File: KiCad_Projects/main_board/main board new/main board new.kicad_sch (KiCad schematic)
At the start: 71 parts

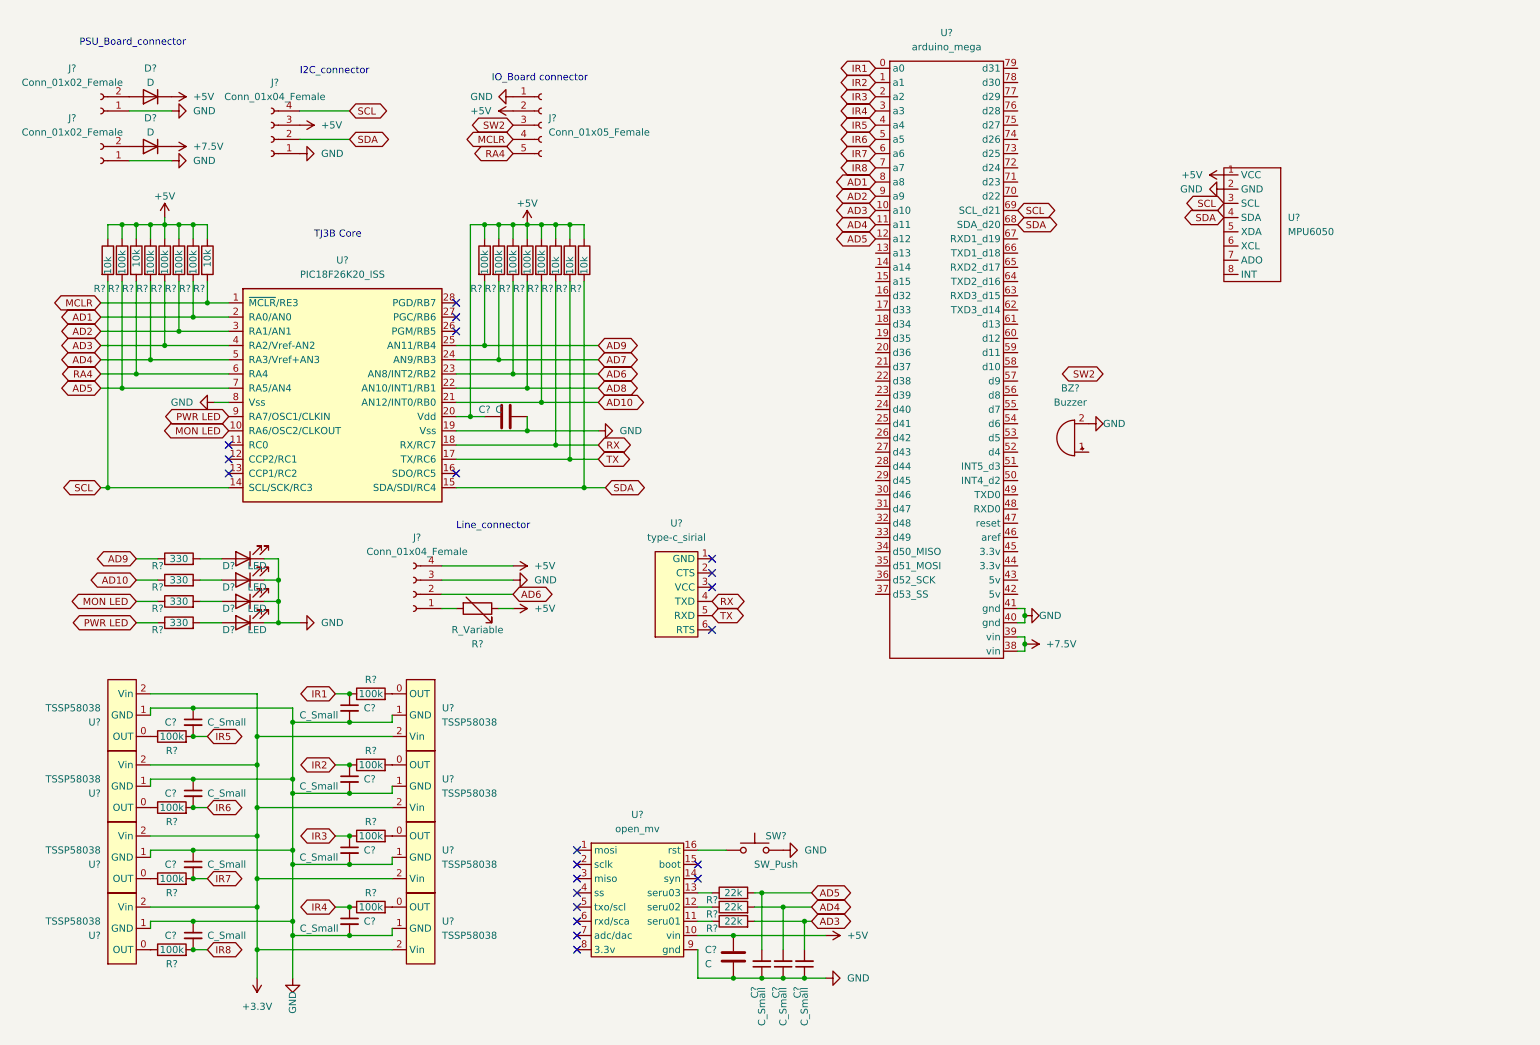
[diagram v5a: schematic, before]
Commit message: 基板データの更新
新メイン基板の更新
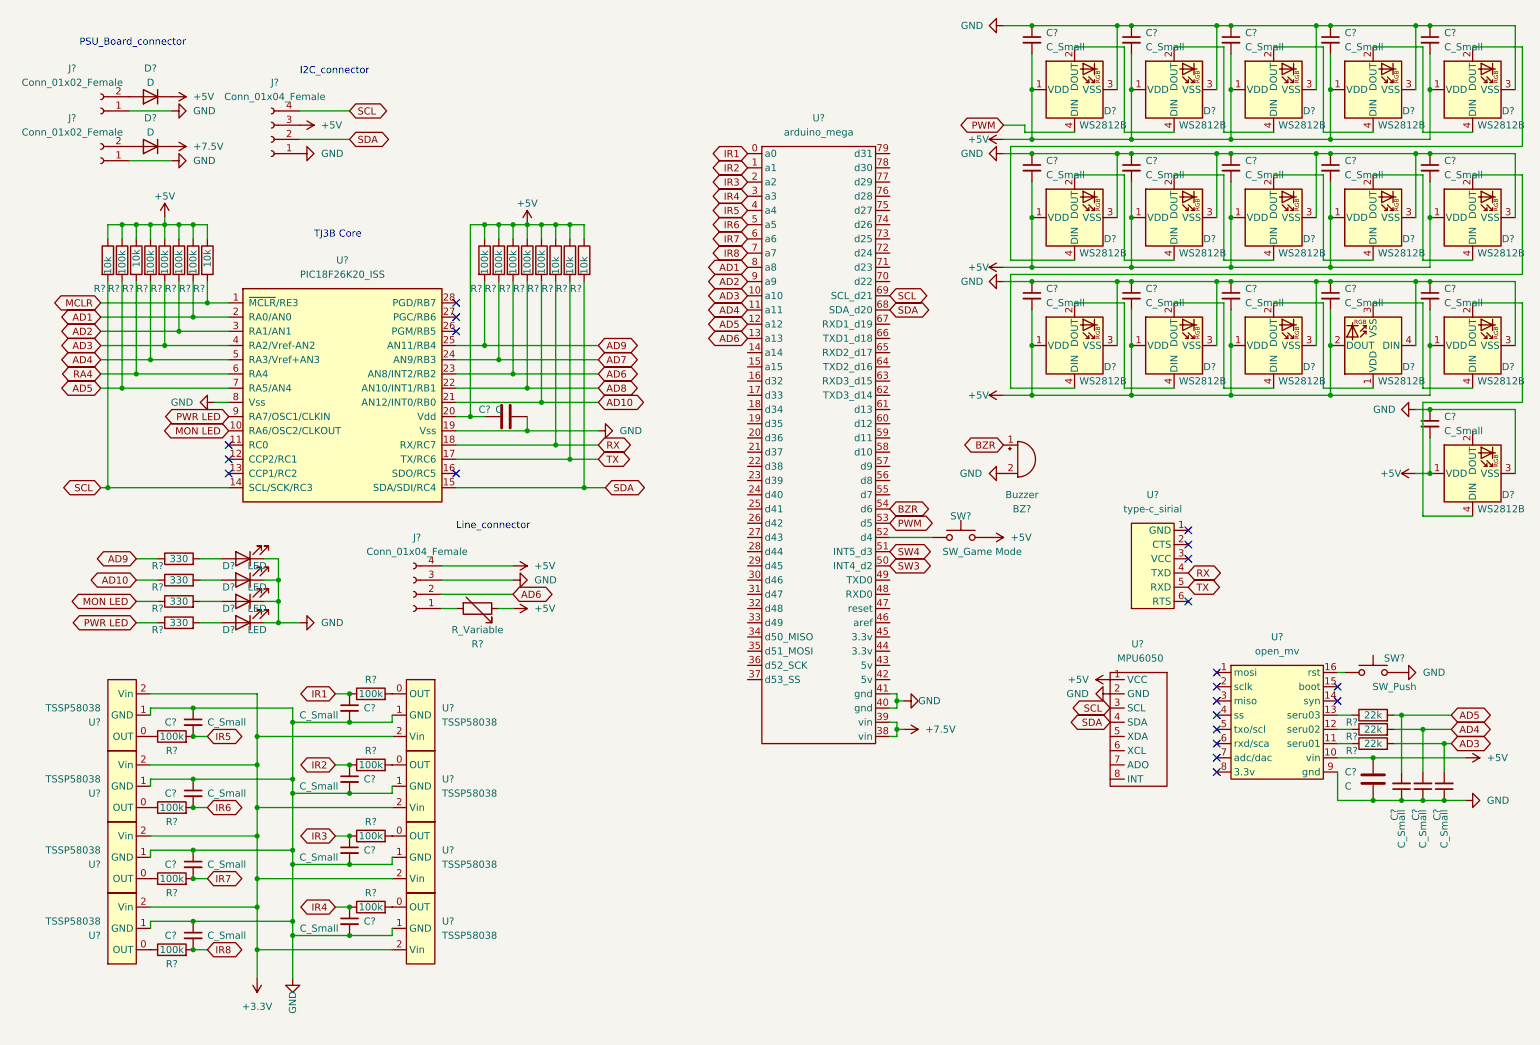
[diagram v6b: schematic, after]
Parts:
- removed J?: Conn_01x05_Female, Connector_JST:JST_XH_B5B-XH-A_1x05_P2.50mm_Vertical, symbol Connector:Conn_01x05_Female
- added C? (x16): C_Small, symbol Device:C_Small
- added D? (x16): WS2812B, LED_SMD:LED_WS2812B_PLCC4_5.0x5.0mm_P3.2mm, symbol LED:WS2812B
- added SW?: SW_Game Mode, Button_Switch_THT:SW_PUSH_6mm_H5mm, symbol Switch:SW_Push
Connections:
- net +5V: now also C?.2, C?.2, C?.2, C?.2, C?.2, C?.2, C?.2, C?.2, C?.2, C?.2, C?.2, C?.2, C?.2, C?.2, C?.2, C?.2, D?.1 (VDD), D?.1 (VDD), D?.1 (VDD), D?.1 (VDD), D?.1 (VDD), D?.1 (VDD), D?.1 (VDD), D?.1 (VDD), D?.1 (VDD), D?.1 (VDD), D?.1 (VDD), D?.1 (VDD), D?.1 (VDD), D?.1 (VDD), D?.1 (VDD), D?.2 (DOUT), SW?.2
- net AD6: now also U?.13 (a13)
- net GND: now also C?.1, C?.1, C?.1, C?.1, C?.1, C?.1, C?.1, C?.1, C?.1, C?.1, C?.1, C?.1, C?.1, C?.1, C?.1, C?.1, D?.3 (VSS), D?.3 (VSS), D?.3 (VSS), D?.3 (VSS), D?.3 (VSS), D?.3 (VSS), D?.3 (VSS), D?.3 (VSS), D?.3 (VSS), D?.3 (VSS), D?.3 (VSS), D?.3 (VSS), D?.3 (VSS), D?.3 (VSS), D?.3 (VSS), D?.4 (DIN)
- net BZR: now reaches BZ?.1 (-)
- net BZR: now also U?.54 (d6)
- net SW3: now reaches U?.50 (INT4_d2)
- net SW4: now reaches U?.51 (INT5_d3)
- net at U?.52 (d4): now also SW?.1
- net PWM: now reaches U?.53 (d5)
- net PWM: now also D?.4 (DIN)
- new net: D?.2 (DOUT), D?.4 (DIN) (x13)
- new net: D?.3 (VSS), D?.4 (DIN)
- new net: D?.1 (VDD), D?.2 (DOUT)
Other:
- note removed: "IO_Board connector"
- moved on the sheet: BZ?, C?, R?, SW?, U?

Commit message: CADデータの追加、更新
各基盤のファイル、データの追加
Fusion360の新ロボの設計のデータ追加
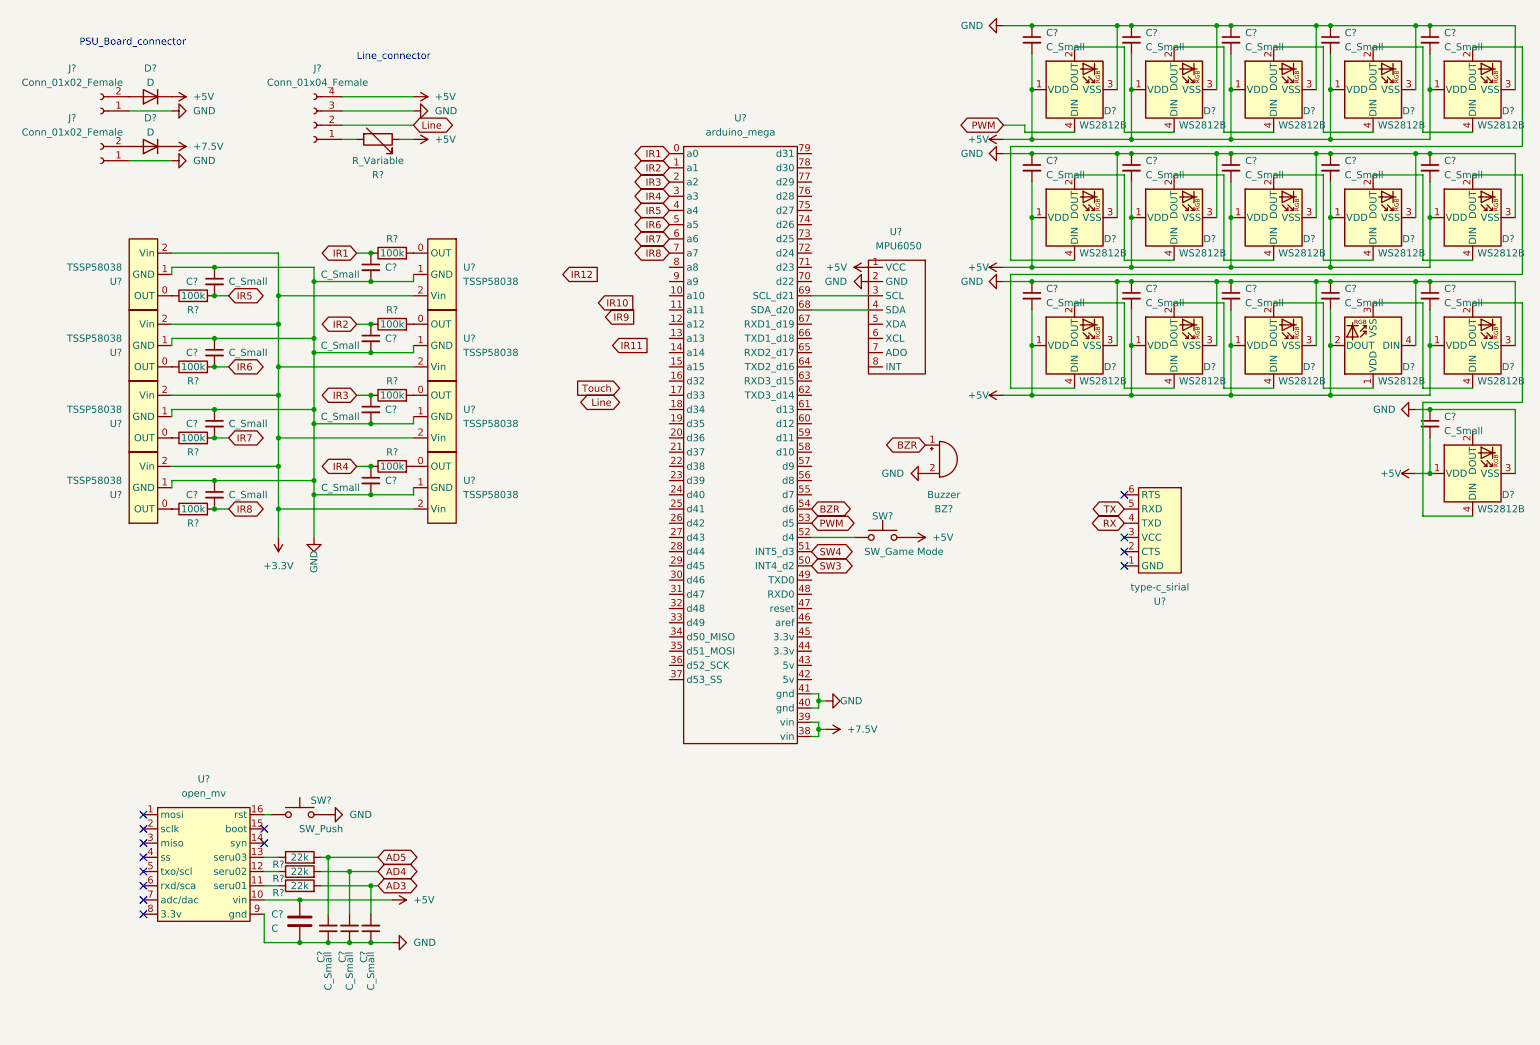
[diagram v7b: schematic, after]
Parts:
- removed C?: C, Capacitor_THT:CP_Radial_D5.0mm_P2.50mm, symbol Device:C
- removed D? (x4): LED, LED_THT:LED_D5.0mm_Clear, symbol Device:LED
- removed J?: Conn_01x04_Female, Connector_JST:JST_XH_B4B-XH-A_1x04_P2.50mm_Vertical, symbol Connector:Conn_01x04_Female
- removed R? (x4): 330, Resistor_THT:R_Axial_DIN0204_L3.6mm_D1.6mm_P5.08mm_Horizontal, symbol Device:R
- removed R? (x10): 100k, Resistor_THT:R_Axial_DIN0204_L3.6mm_D1.6mm_P5.08mm_Horizontal, symbol Device:R
- removed R? (x6): 10k, Resistor_THT:R_Axial_DIN0204_L3.6mm_D1.6mm_P5.08mm_Horizontal, symbol Device:R
- removed U?: PIC18F26K20_ISS, Package_DIP:DIP-28_W7.62mm_Socket_LongPads, symbol tj3b pic:PIC18F26K20_ISS
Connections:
- net AD3: no longer U?.10 (a10)
- net AD4: no longer U?.11 (a11)
- net AD5: no longer U?.12 (a12)
- net AD1: no longer names the net of U?.8 (a8)
- net AD2: no longer names the net of U?.9 (a9)
- net AD6: no longer names the net of U?.13 (a13)
- net AD6: no longer J?.2 (Pin_2)
- net SCL: no longer names the net of U?.3 (SCL), U?.69 (SCL_d21)
- net SDA: no longer names the net of U?.4 (SDA), U?.68 (SDA_d20)
- new net Line: J?.2 (Pin_2)
- no-connect marks 21 -> 14
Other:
- note removed: "I2C_connector"
- note removed: "TJ3B Core"
- moved on the sheet: BZ?, C?, J?, R?, SW?, U?
